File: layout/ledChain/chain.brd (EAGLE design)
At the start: 32.5 x 21.3 mm, 29 parts, among them IC2 FT232RL, P1 FSM4JSMA-SMD, T1 BC848, T2 BC848

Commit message: not quite their
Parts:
- removed IC1: (no value), sid:SOT223
- removed P1: FSM4JSMA-SMD, switch-misc:FSM4JSMA-SMD
- removed R19: 10k, rcl-2:R0603
- removed U$40: USB-B, sid:USB-MICROB
- added C8: 100n, rcl:C0603
- added IC3: ATTINY10, adafruit:SOT23-6
- added S1: DTSM-3, switch-tact:DTSM-3
- added U1: SPX3819M5-L-3-3, ESP8266-2:SOT95P280X145-5N
- C1, C6: value 100u -> 68u 6.3V Tantal Poly; device cap-master:7343-TE-D -> rcl-2:C0805
- U$3: value ATTINY45 -> USB-MALE-SMT; device SparkFun:SO08-EIAJ -> sid:USB-MALE-SMT
- moved R2 33.6 mm to (69.3, 55.4), flipped to the bottom, turned to 180 degrees
- moved C6 30.3 mm to (71.9, 60.5), flipped to the bottom, turned to 90 degrees
- moved U$3 28.1 mm to (48.3, 55.9), flipped to the top
- moved T1 24.6 mm to (64.3, 60.5)
- moved C1 24.3 mm to (59.2, 50.5), turned to 90 degrees
- moved SJ1 23.5 mm to (71.4, 50.0), flipped to the bottom
- moved U$2 23.5 mm to (78.0, 62.0), turned to 180 degrees
- moved U$1 22.4 mm to (66.0, 53.1), flipped to the bottom, turned to 270 degrees
- moved R3 21.3 mm to (66.8, 57.4), turned to 270 degrees
- moved C2 20.5 mm to (55.4, 49.8), turned to 0 degrees
- moved IC2 19.9 mm to (57.7, 56.1)
- moved R4 19.0 mm to (64.0, 57.9), turned to 180 degrees
- moved C5 17.9 mm to (56.9, 50.8), turned to 90 degrees
- moved SV2 17.7 mm to (74.9, 57.1)
- moved C4 16.8 mm to (50.3, 53.1), turned to 90 degrees
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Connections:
- removed net N$12: C2.1, IC2.17
- removed net N$2: R19.1, U$2.CH_PD
- new net N$15: C2.1, IC2.17, IC2.4
- new net N$17: C8.1, U1.4
- net +3V3: now also C6.1, U$2.CH_PD, U1.5; no longer C6.+, IC1.2, IC1.4, IC2.4, R19.2
- net +5V: now also C1.1, IC3.5, U$3.VBUS1, U1.1, U1.3; no longer C1.+, IC1.3, U$3.8, U$40.VBUS
- net GND: now also C1.2, C6.2, C8.2, IC3.2, S1.2, U$3.GND1, U$3.S1, U$3.S2, U1.2; no longer C1.-, C6.-, IC1.1, P1.P$3, P1.P$4, U$3.4, U$40.GND, U$40.MT1, U$40.MT2
- net GPIO0: now also S1.1; no longer P1.P$1, P1.P$2
- net N$10: now also IC3.1, SV2.P$2; no longer R5.1, U$3.7
- net N$11: now also IC3.6, R2.1; no longer SV2.P$2, U$3.6
- net N$13: now also IC3.3; no longer U$3.2
- net N$14: now also R5.1; no longer R5.2
- net N$3: now also U$3.D+1; no longer U$40.D+
- net N$4: now also U$3.D-1; no longer U$40.D-
- net N$6: now also IC3.4, R5.2; no longer R2.1, U$3.1
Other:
- board size 32.5 x 21.3 mm -> 28.2 x 15.7 mm

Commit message: before ws281x converter
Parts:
- added IC4: ATTINY85-20S, avr:SOIC8
- moved U$2 4.06 mm to (82.0, 62.0)
- moved SV2 2.03 mm to (77.0, 57.1)
- moved S1 0.36 mm to (57.1, 56.4)
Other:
- board size 28.2 x 15.7 mm -> 30 x 15.7 mm
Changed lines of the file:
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@@
 <board>
 <plain>
-<wire x1="49.022" y1="48.006" x2="77.196" y2="48.006" width="0" layer="20"/>
-<wire x1="77.196" y1="48.006" x2="77.196" y2="63.678" width="0" layer="20"/>
-<wire x1="77.196" y1="63.678" x2="49.022" y2="63.678" width="0" layer="20"/>
+<wire x1="49.022" y1="48.006" x2="78.974" y2="48.006" width="0" layer="20"/>
+<wire x1="78.974" y1="48.006" x2="78.974" y2="63.678" width="0" layer="20"/>
+<wire x1="78.974" y1="63.678" x2="49.022" y2="63.678" width="0" layer="20"/>
 <wire x1="49.022" y1="63.678" x2="49.022" y2="48.006" width="0" layer="20"/>
 </plain>
@@
 <element name="R4" library="rcl-2" package="R0603" value="10k" x="64.008" y="57.912" rot="MR180"/>
 <element name="R5" library="rcl-2" package="R0603" value="470" x="63.754" y="50.038" rot="MR90"/>
-<element name="S1" library="switch-tact" package="DTSM-3" value="DTSM-3" x="57.404" y="56.642" rot="R90"/>
+<element name="S1" library="switch-tact" package="DTSM-3" value="DTSM-3" x="57.15" y="56.388" rot="R90"/>
 <element name="SJ1" library="jumper" package="SJ_2" value="" x="71.374" y="50.038" rot="MR180"/>
-<element name="SV2" library="sid" package="1X4SMD-2.54LIEGEND" value="1X4SMD-2.54LIEGEND" x="74.93" y="57.15" rot="MR90"/>
+<element name="SV2" library="sid" package="1X4SMD-2.54LIEGEND" value="1X4SMD-2.54LIEGEND" x="76.962" y="57.15" rot="MR90"/>
 <element name="T1" library="transistor-neu-to92" package="SOT23" value="BC848" x="64.262" y="60.452" rot="MR90"/>
 <element name="T2" library="transistor-neu-to92" package="SOT23" value="BC848" x="64.262" y="55.372" rot="MR90"/>
 <element name="U$1" library="m-pad-1.5" package="SOT23" value="BSS138" x="66.04" y="53.086" rot="MR270"/>
-<element name="U$2" library="ESP8266" package="ESP-03" value="ESP8266" x="77.978" y="61.976" rot="R180"/>
+<element name="U$2" library="ESP8266" package="ESP-03" value="ESP8266" x="82.042" y="61.976" rot="R180"/>
 <element name="U$3" library="sid" package="USB-MALE-SMT" value="USB-MALE-SMT" x="48.26" y="55.88" rot="R90"/>
 <element name="U1" library="ESP8266-2" package="SOT95P280X145-5N" value="SPX3819M5-L-3-3" x="69.342" y="60.452" rot="MR270">
@@
 <attribute name="OC_FARNELL" value="1831949" x="69.342" y="60.452" size="1.778" layer="28" rot="MR270" display="off"/>
 </element>
+<element name="IC4" library="avr" package="SOIC8" value="ATTINY85-20S" x="61.722" y="56.388"/>
 </elements>
 <signals>
@@
 <wire x1="70.192" y1="55.372" x2="70.2818" y2="61.6204" width="0" layer="19" extent="16-16"/>
 <wire x1="69.058" y1="52.832" x2="70.192" y2="55.372" width="0" layer="19" extent="16-16"/>
-<wire x1="74.93" y1="52.07" x2="70.192" y2="55.372" width="0" layer="19" extent="16-16"/>
+<wire x1="76.962" y1="52.07" x2="70.192" y2="55.372" width="0" layer="19" extent="16-16"/>
 <wire x1="61.722" y1="49.188" x2="69.058" y2="52.832" width="0" layer="19" extent="16-16"/>
 <wire x1="59.182" y1="49.596" x2="61.722" y2="49.188" width="0" layer="19" extent="1-16"/>
@@
 <contactref element="C8" pad="2"/>
 <wire x1="69.342" y1="61.6204" x2="71.882" y2="61.402" width="0" layer="19" extent="16-16"/>
-<wire x1="74.93" y1="59.69" x2="71.882" y2="61.402" width="0" layer="19" extent="16-16"/>
+<wire x1="76.962" y1="59.69" x2="71.882" y2="61.402" width="0" layer="19" extent="16-16"/>
 <wire x1="68.492" y1="57.404" x2="69.342" y2="61.6204" width="0" layer="19" extent="16-16"/>
 <wire x1="71.882" y1="56.046" x2="68.492" y2="57.404" width="0" layer="19" extent="16-16"/>
@@
 <wire x1="67.14" y1="52.136" x2="71.658" y2="52.832" width="0" layer="19" extent="16-16"/>
 <wire x1="65.786" y1="49.188" x2="67.14" y2="52.136" width="0" layer="19" extent="16-16"/>
-<wire x1="61.978" y1="49.576" x2="65.786" y2="49.188" width="0" layer="19" extent="1-16"/>
-<wire x1="59.182" y1="51.496" x2="61.978" y2="49.576" width="0" layer="19" extent="1-1"/>
+<wire x1="66.042" y1="49.576" x2="65.786" y2="49.188" width="0" layer="19" extent="1-16"/>
+<wire x1="59.182" y1="51.496" x2="66.042" y2="49.576" width="0" layer="19" extent="1-1"/>
 <wire x1="56.896" y1="51.65" x2="59.182" y2="51.496" width="0" layer="19" extent="1-1"/>
 <wire x1="54.522" y1="49.784" x2="56.896" y2="51.65" width="0" layer="19" extent="1-16"/>
@@
 <wire x1="54.522" y1="61.722" x2="54.47" y2="59.38" width="0" layer="19" extent="1-1"/>
 <wire x1="51.9176" y1="61.722" x2="54.522" y2="61.722" width="0" layer="19" extent="1-1"/>
-<wire x1="57.404" y1="59.342" x2="54.47" y2="59.38" width="0" layer="19" extent="1-1"/>
+<wire x1="57.15" y1="59.088" x2="54.47" y2="59.38" width="0" layer="19" extent="1-1"/>
 <wire x1="50.292" y1="53.936" x2="50.204" y2="55.626" width="0" layer="19" extent="16-16"/>
-<wire x1="61.283" y1="56.459" x2="57.404" y2="59.342" width="0" layer="19" extent="1-16"/>
+<wire x1="61.283" y1="56.459" x2="57.15" y2="59.088" width="0" layer="19" extent="1-16"/>
 </signal>
 <signal name="+3V3">
@@
 <contactref element="C7" pad="1"/>
 <contactref element="U$2" pad="CH_PD"/>
-<wire x1="71.882" y1="59.502" x2="73.978" y2="62.176" width="0" layer="19" extent="1-16"/>
+<wire x1="71.882" y1="59.502" x2="78.042" y2="62.176" width="0" layer="19" extent="1-16"/>
 <wire x1="71.882" y1="57.746" x2="71.882" y2="59.502" width="0" layer="19" extent="16-16"/>
 <wire x1="68.4022" y1="59.2836" x2="71.882" y2="59.502" width="0" layer="19" extent="16-16"/>
 <wire x1="67.056" y1="59.856" x2="68.4022" y2="59.2836" width="0" layer="19" extent="16-16"/>
 <wire x1="67.818" y1="50.888" x2="71.882" y2="57.746" width="0" layer="19" extent="16-16"/>
-<wire x1="71.978" y1="49.576" x2="67.818" y2="50.888" width="0" layer="19" extent="1-16"/>
+<wire x1="76.042" y1="49.576" x2="67.818" y2="50.888" width="0" layer="19" extent="1-16"/>
 <wire x1="57.824" y1="61.722" x2="67.056" y2="59.856" width="0" layer="19" extent="1-16"/>
 </signal>
@@
 <wire x1="65.786" y1="50.888" x2="65.362" y2="60.452" width="0" layer="19" extent="16-16"/>
 <wire x1="67.818" y1="49.188" x2="65.786" y2="50.888" width="0" layer="19" extent="16-16"/>
-<wire x1="69.978" y1="49.576" x2="67.818" y2="49.188" width="0" layer="19" extent="1-16"/>
+<wire x1="74.042" y1="49.576" x2="67.818" y2="49.188" width="0" layer="19" extent="1-16"/>
 </signal>
 <signal name="GPIO0">
@@
 <contactref element="R23" pad="1"/>
 <contactref element="S1" pad="1"/>
-<wire x1="59.524" y1="61.722" x2="61.978" y2="62.176" width="0" layer="19" extent="1-1"/>
-<wire x1="65.362" y1="55.372" x2="61.978" y2="62.176" width="0" layer="19" extent="1-16"/>
-<wire x1="57.404" y1="53.942" x2="59.524" y2="61.722" width="0" layer="19" extent="1-1"/>
+<wire x1="59.524" y1="61.722" x2="66.042" y2="62.176" width="0" layer="19" extent="1-1"/>
+<wire x1="65.362" y1="55.372" x2="66.042" y2="62.176" width="0" layer="19" extent="1-16"/>
+<wire x1="57.15" y1="53.688" x2="59.524" y2="61.722" width="0" layer="19" extent="1-1"/>
 </signal>
 <signal name="TX">
 <contactref element="IC2" pad="5"/>
 <contactref element="U$2" pad="UTXD"/>
-<wire x1="65.978" y1="49.576" x2="61.283" y2="57.759" width="0" layer="19" extent="1-16"/>
+<wire x1="70.042" y1="49.576" x2="61.283" y2="57.759" width="0" layer="19" extent="1-16"/>
 </signal>
 <signal name="RX">
 <contactref element="IC2" pad="1"/>
 <contactref element="U$2" pad="URXD"/>
-<wire x1="67.978" y1="49.576" x2="61.283" y2="60.359" width="0" layer="19" extent="1-16"/>
+<wire x1="72.042" y1="49.576" x2="61.283" y2="60.359" width="0" layer="19" extent="1-16"/>
 </signal>
 <signal name="GPIO15">
 <contactref element="U$2" pad="GPIO15"/>
 <contactref element="R22" pad="2"/>
-<wire x1="56.222" y1="61.722" x2="65.978" y2="62.176" width="0" layer="19" extent="1-1"/>
+<wire x1="56.222" y1="61.722" x2="70.042" y2="62.176" width="0" layer="19" extent="1-1"/>
 </signal>
 <signal name="GPIO2">
@@
 <contactref element="U$2" pad="GPIO2"/>
 <contactref element="R21" pad="1"/>
-<wire x1="63.978" y1="62.176" x2="67.056" y2="61.556" width="0" layer="19" extent="1-16"/>
+<wire x1="68.042" y1="62.176" x2="67.056" y2="61.556" width="0" layer="19" extent="1-16"/>
 <wire x1="67.14" y1="54.036" x2="67.056" y2="61.556" width="0" layer="19" extent="16-16"/>
 </signal>
@@
 <contactref element="SJ1" pad="2"/>
 <contactref element="SV2" pad="P$3"/>
-<wire x1="71.374" y1="50.038" x2="74.93" y2="57.15" width="0" layer="19" extent="16-16"/>
+<wire x1="71.374" y1="50.038" x2="76.962" y2="57.15" width="0" layer="19" extent="16-16"/>
 </signal>
 <signal name="N$6">
@@
 <contactref element="IC3" pad="1"/>
 <contactref element="SV2" pad="P$2"/>
-<wire x1="71.658" y1="53.782" x2="74.93" y2="54.61" width="0" layer="19" extent="16-16"/>
+<wire x1="71.658" y1="53.782" x2="76.962" y2="54.61" width="0" layer="19" extent="16-16"/>
 </signal>
 <signal name="N$17">

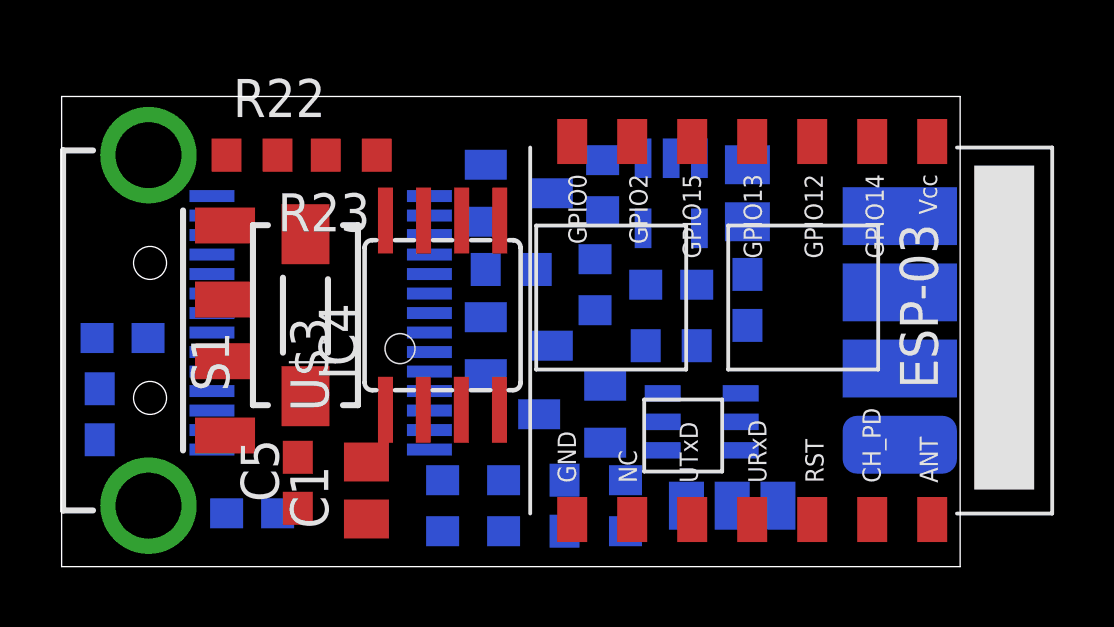
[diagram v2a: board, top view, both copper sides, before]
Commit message: power rails done
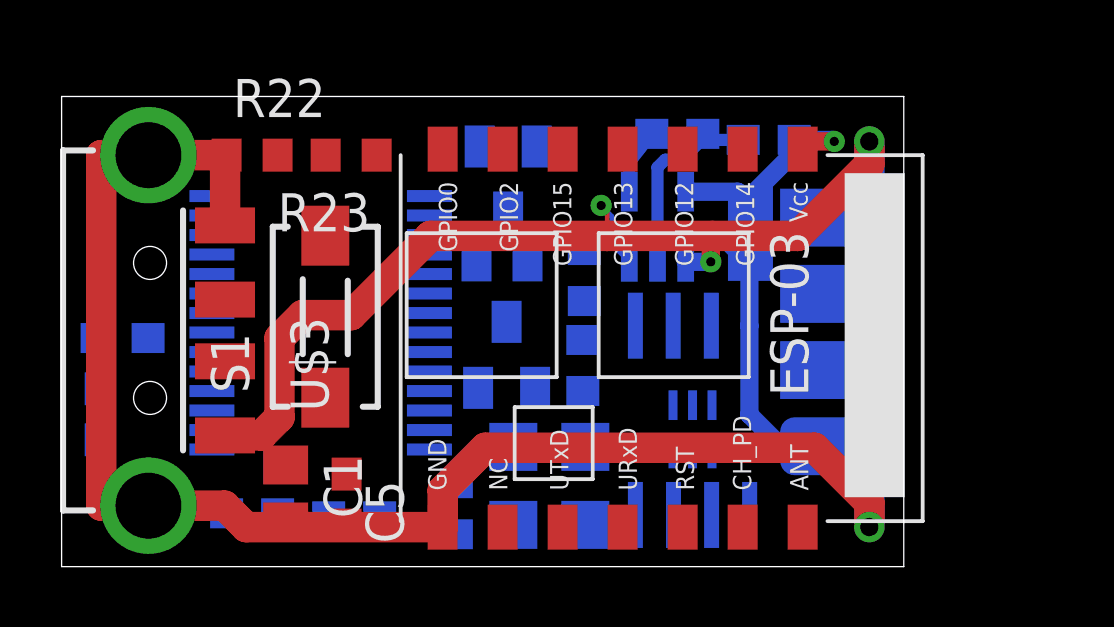
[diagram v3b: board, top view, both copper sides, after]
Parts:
- removed IC3: ATTINY10, adafruit:SOT23-6
- removed R1, R5: 470, rcl-2:R0603
- removed R2: 10k, rcl-2:R0603
- removed SJ1: (no value), jumper:SJ_2
- removed SV2: 1X4SMD-2.54LIEGEND, sid:1X4SMD-2.54LIEGEND
- added Q1: 25mhz, sid:KC5032A
- added SV1: 1X4SMD-2.54LIEGEND, sid:1X4SMD-2.54LIEGEND
- U$1: value BSS138 -> 74HCT2G14GWQ100; device m-pad-1.5:SOT23 -> sid:SOT363
- moved IC4 9.04 mm to (70.1, 52.9), flipped to the bottom, turned to 180 degrees
- moved C9 7.02 mm to (58.8, 49.7), turned to 0 degrees
- moved R21 6.03 mm to (66.4, 54.7), turned to 90 degrees
- moved R20 5.64 mm to (62.2, 49.9)
- moved C7 5.38 mm to (72.6, 62.2), turned to 0 degrees
- moved C8 5.03 mm to (69.5, 62.4), turned to 180 degrees
- moved U$2 4.33 mm to (77.7, 61.7)
- moved U$1 4.05 mm to (70.1, 52.6), turned to 0 degrees
- moved C1 2.69 mm to (56.5, 50.4), turned to 270 degrees
- moved C5 1.72 mm to (58.5, 50.2), turned to 270 degrees
- moved C6 1.32 mm to (72.0, 59.1), turned to 270 degrees
- moved U1 1.21 mm to (68.9, 59.3), turned to 90 degrees
- moved S1 0.66 mm to (57.8, 56.3)
- moved T1 0.58 mm to (63.9, 60.9), turned to 180 degrees
- moved T2 0.51 mm to (63.9, 55.1), turned to 0 degrees
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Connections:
- removed net N$10: IC3.1, SV2.P$2
- removed net N$11: IC3.6, R2.1
- removed net N$13: IC3.3, SJ1.3
- removed net N$14: R1.1, R5.1, SJ1.1, U$1.3
- removed net N$6: IC3.4, R5.2
- removed net N$9: SJ1.2, SV2.P$3
- new net N$2: IC4.2, Q1.P$3
- new net WSCLK: IC4.5, SV1.P$3, U$1.6
- new net WSDATA: IC4.6, SV1.P$2, U$1.4
- net +5V: now also IC4.8, Q1.P$4, SV1.P$4, U$1.5; no longer IC3.5, R1.2, R2.2, SV2.P$1
- net GND: now also IC4.4, Q1.P$2, SV1.P$1; no longer IC3.2, SV2.P$4
- net GPIO15: now also IC4.3
- net GPIO2: now also IC4.7, U$1.3
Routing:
- net GND: track 0.00 -> 70.1 mm, vias 0 -> 1
- net +5V: track 0.00 -> 36.2 mm, vias 0 -> 3
- net +3V3: track 0.00 -> 7.60 mm, vias 0 -> 1
- net N$17: track 0.00 -> 2.19 mm
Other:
- board size 30 x 15.7 mm -> 28.1 x 15.7 mm

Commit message: challenge accepted and passed
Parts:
- added C10: 100n, rcl:C0603
- moved R20 1.18 mm to (61.0, 49.8), turned to 0 degrees
- moved C9 0.76 mm to (58.0, 49.7)
- moved S1 0.59 mm to (58.0, 55.8), turned to 270 degrees
- moved C3 0.53 mm to (50.9, 56.1)
- moved C4 0.53 mm to (50.1, 53.6)
- moved Q1 0.43 mm to (64.8, 50.7)
- moved U$1 0.41 mm to (69.6, 52.6), turned to 90 degrees
- moved C2 0.37 mm to (55.0, 49.9)
- moved R23 0.30 mm to (58.5, 61.5), turned to 0 degrees
- moved C7 0.21 mm to (72.5, 62.4)
- moved IC4 0.21 mm to (70.3, 52.8)
- moved C1 0.20 mm to (56.3, 50.4)
- moved C5 0.20 mm to (58.3, 50.2)
- moved R3 0.20 mm to (66.2, 57.7)
- moved T1 0.20 mm to (63.9, 60.7)
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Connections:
- net +3V3: now also C10.1, IC2.4
- net GND: now also C10.2
- net N$15: no longer IC2.4
- net WSCLK: now also U$1.4; no longer U$1.6
- net WSDATA: now also U$1.6; no longer U$1.4
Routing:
- net +3V3: track 7.60 -> 60.7 mm, vias 1 -> 6
- net GND: track 70.1 -> 122.9 mm, vias 1 -> 4
- net RST: track 0.00 -> 25.5 mm, vias 0 -> 1
- net +5V: track 36.2 -> 60.8 mm, vias 3 -> 6
- net TX: track 0.00 -> 22.4 mm, vias 0 -> 1
- net GPIO0: track 0.00 -> 21.7 mm, vias 0 -> 1
- net GPIO15: track 0.00 -> 21.3 mm, vias 0 -> 1
- net RX: track 0.00 -> 19.9 mm, vias 0 -> 3
- net GPIO2: track 0.00 -> 19.1 mm, vias 0 -> 3
- net N$1: track 0.00 -> 15.1 mm
- net WSCLK: track 0.00 -> 12.6 mm, vias 0 -> 2
- net N$3: track 0.00 -> 12.2 mm, vias 0 -> 1
- net WSDATA: track 0.00 -> 8.73 mm, vias 0 -> 2
- net N$5: track 0.00 -> 7.54 mm
- net N$4: track 0.00 -> 7.36 mm, vias 0 -> 1
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- added copper zone on layer 1, net GND
- added copper zone on layer 16, net GND
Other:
- board size 28.1 x 15.7 mm -> 27.2 x 15.7 mm

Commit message: added doku layer
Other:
- board text added: "+"
- board text added: "-"
- board text added: "v1.0"
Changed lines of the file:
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@@
 <vertex x="75.4888" y="51.6636"/>
 </polygon>
+<text x="75.3872" y="60.7568" size="0.9144" layer="48" font="vector" ratio="18" rot="MR0">+</text>
+<text x="75.4126" y="49.8348" size="0.9144" layer="48" font="vector" ratio="18" rot="MR0">-</text>
+<text x="52.6542" y="59.3598" size="0.9144" layer="48" font="vector" ratio="18" rot="MR0">v1.0</text>
 </plain>
 <attributes>

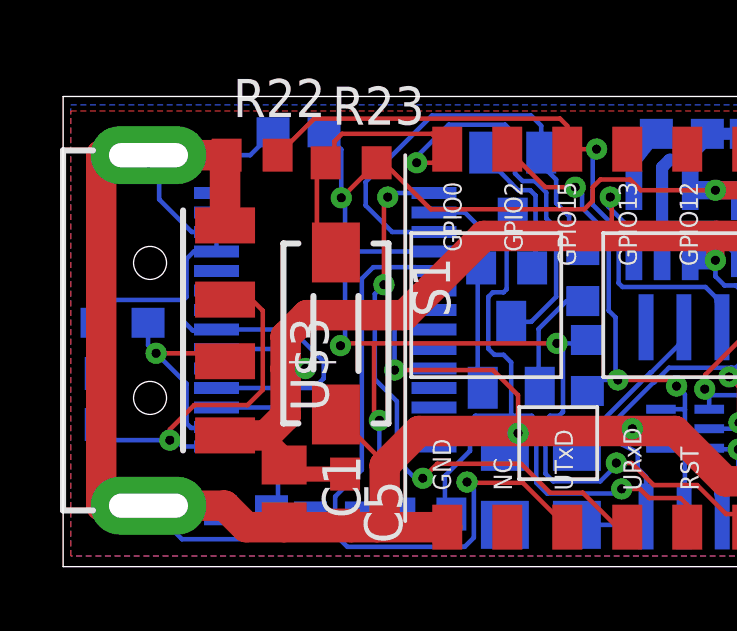
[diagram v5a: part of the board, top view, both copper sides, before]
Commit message: Schaltplan für ledChain hinzugefügt. Bauteilbezeichnungen sortiert.
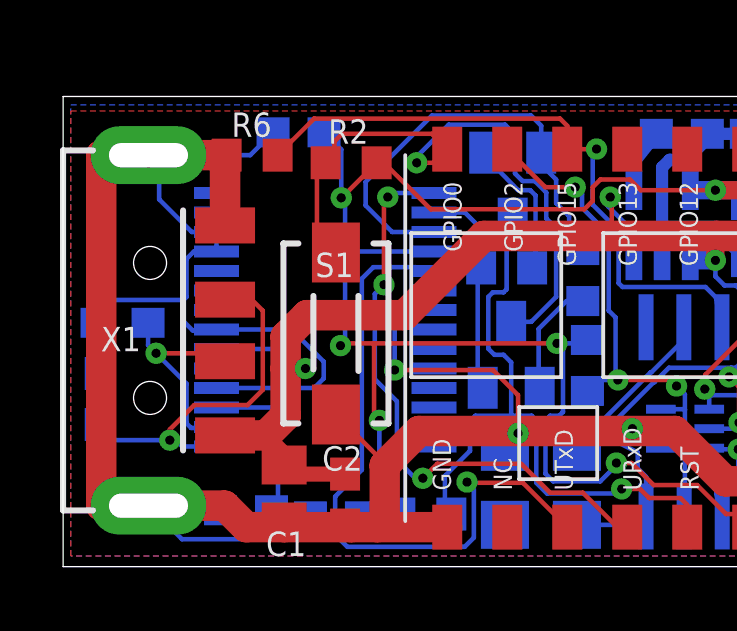
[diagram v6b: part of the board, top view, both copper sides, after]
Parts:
- removed R21: 10k, rcl-2:R0603
- added R5: 10k, rcl-2:R0603
- C3, C4: value 22p -> 100n
- C5: value 100n -> 68u 6.3V Tantal Poly; device rcl:C0603 -> rcl-2:C0805
- C6: value 68u 6.3V Tantal Poly -> 100n; device rcl-2:C0805 -> rcl:C0603
- C8, C9: value 100n -> 22p
- moved C4 24.1 mm to (72.5, 62.4), turned to 0 degrees
- moved C3 19.7 mm to (69.5, 62.4), turned to 180 degrees
- moved C8 19.7 mm to (50.9, 56.1), turned to 0 degrees
- moved C7 19.3 mm to (58.0, 49.7)
- moved C5 16.3 mm to (71.9, 59.3), flipped to the bottom
- moved C6 15.5 mm to (56.8, 62.5), turned to 0 degrees
- moved C10 12.7 mm to (55.0, 49.9)
- moved C9 8.79 mm to (50.1, 53.6), turned to 90 degrees
- moved T1 5.64 mm to (63.9, 55.1), turned to 0 degrees
- moved T2 5.64 mm to (63.9, 60.7), turned to 180 degrees
- moved C2 3.32 mm to (58.3, 50.2), flipped to the top, turned to 270 degrees
- moved R3 3.00 mm to (66.4, 54.7), turned to 90 degrees
- moved R4 2.55 mm to (66.2, 57.7), turned to 270 degrees
- renumbered IC4 to IC1, R20 to R1, R22 to R6, R23 to R2, U$1 to IC3, U$3 to X1
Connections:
- removed net N$7 (its old number): R3.2, T2.1
- new net N$8: R5.2, T2.1
- net +3V3: now also C4.1, C5.1, R3.2; no longer C10.1, C7.1, R21.2
- net +5V: now also C2.1; no longer C5.1
- net GPIO0: now also T1.3; no longer T2.3
- net GPIO2: now also R3.1; no longer R21.1
- net N$1: now also R4.1, T2.2; no longer R3.1, T1.2
- net N$15: now also C10.1; no longer C2.1
- net N$17: now also C3.1; no longer C8.1
- net N$3: now also C9.1; no longer C4.1
- net N$4: now also C8.1; no longer C3.1
- net N$5: now also R5.1, T1.2; no longer R4.1, T2.2
- net RST: now also C7.1, T2.3; no longer C9.1, T1.3
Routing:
- net N$8: track 0.00 -> 4.84 mm
- net N$7 (its old number): track 3.84 -> 0.00 mm
- net N$7: track 4.84 -> 3.84 mm
